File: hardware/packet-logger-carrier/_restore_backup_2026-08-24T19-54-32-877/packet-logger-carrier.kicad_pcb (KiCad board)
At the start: 2 copper layers, 86 x 58 mm, 22 parts, among them J1 RAK19003 J6, J10 RAK SPARE, J11 ESP SPARE, J12 BATT IN, J13 BATT JST-PH, J14 BATT TO RAK, J15 J15, J2 RAK19003 J7, J3 XIAO ESP32-C6, J4 microSD, J5 LID CABLE, SW1 USER BUTTON, SW2 POWER SWITCH

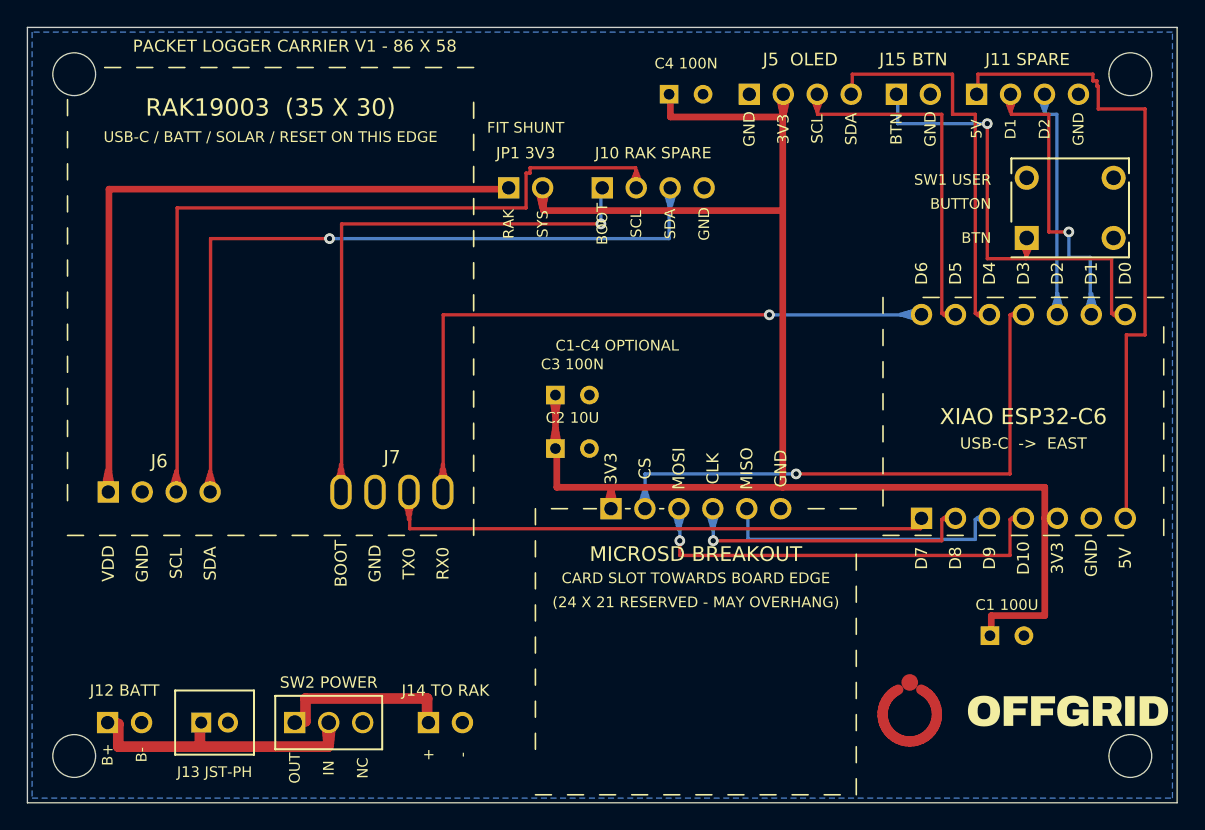
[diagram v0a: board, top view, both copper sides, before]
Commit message: hardware: add teardrops and make the router prefer roomy paths
Two more rounds of the same concern - traces sitting close to pads, and joints
meeting pads at what looked like an angle. Both now addressed properly.

TEARDROPS (src/teardrops.py)
Flares the trace where it meets a pad, built from real track segments on the
same net so KiCad connectivity and our DRC treat them as ordinary copper. This
removes the acute trace/pad corner entirely and puts metal at the joint.

Three bugs found while building it, each caught by a check rather than by eye:

  - the flare ran straight on past where the trace turned, landing on whatever
    was next door: 41 clearance violations. Now clamped to its own segment.
  - the span was measured from the track endpoint rather than the pad centre,
    which are not the same point, so one flare overshot: 1 dangling end.
  - a flare was generated from a segment that merely PASSED NEAR a pad rather
    than terminating in it, leaving copper floating beside the trace. Now
    requires the segment to run through the pad centre (perp <= 0.08 mm).

Also splits the underlying trace at each flare tip so the tip meets a real
vertex - without that KiCad reported 14 dangling ends.

ROOMIER ROUTING
The router now pays a cost for cells within 0.22 mm of foreign copper: still
legal, just discouraged, so traces drift to the middle of a gap instead of
hugging one edge. Free - same 8 vias, one extra segment.

Measured on the pads that prompted this:

    pad 13 (D1)   0.397 -> 0.597 mm
    pad 14 (D0)   0.355 -> 0.555 mm

Board-wide clearance distribution, before -> after:
    0.30-0.40 mm    74 -> 2
    0.40-0.60 mm     8 -> 58
    0.60 mm plus   188 -> 517

Worth recording for the record: none of this was necessary for manufacture.
The tightest spot was already 2.4x the 0.127 mm fab minimum, and every one of
those traces runs under soldermask, so solder cannot bridge to them. It is a
better board, not a rescued one.

All gates pass. KiCad 10 DRC: 0 erro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
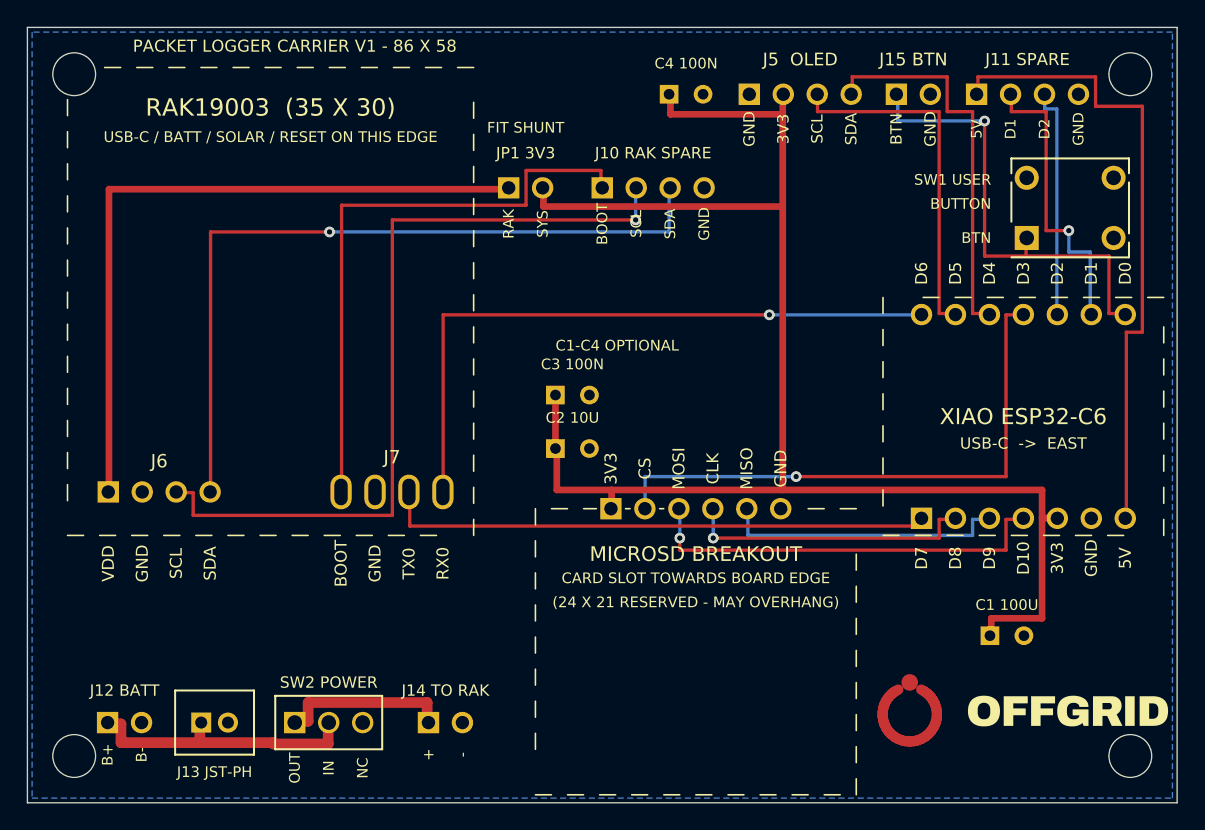
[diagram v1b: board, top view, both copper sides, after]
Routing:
- net +3V3: track 127.4 -> 118.6 mm
- net RAK_RX0: track 52.1 -> 48.5 mm
- net SD_MOSI: track 34.1 -> 30.9 mm
- net RAK_TX0: track 43.9 -> 40.8 mm
- net RAK_SDA: track 60.0 -> 56.9 mm
- net XIAO_D1: track 25.0 -> 22.2 mm
- net XIAO_D2: track 20.0 -> 17.2 mm
- net SD_CLK: track 24.4 -> 21.6 mm
- net SD_CS: track 45.0 -> 42.6 mm
- net BTN: track 37.0 -> 34.6 mm
- net RAK_SCL: track 62.7 -> 60.4 mm, vias 0 -> 1
- net BAT+: track 23.0 -> 20.8 mm
- net OLED_SCL: track 28.7 -> 26.6 mm
- net RAW_3V3: track 53.9 -> 52.4 mm
- net SD_MISO: track 22.6 -> 21.1 mm
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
